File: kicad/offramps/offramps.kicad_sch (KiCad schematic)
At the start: 211 parts, among them J10 Conn_01x04_Socket, J11 Screw_Terminal_01x02, J12 Conn_01x04_Pin, J13 Micro_SD_Card, J14 Conn_01x03_Male, J15 Screw_Terminal_01x02, J16 Conn_01x02_Pin, J17 Conn_01x02_Pin, J3 VITA_57.1_FMC_HPC_Carrier, J4 Conn_01x02_Pin, J5 Conn_Coaxial, J6 Conn_01x03_Male, J7 Conn_Coaxial, J8 Conn_Coaxial, J9 Conn_01x06_Male, Q1 BSS138, Q10 BSS138, Q11 BSS138, Q12 BSS138, Q13 NPN, Q14 NPN, Q15 NPN, Q16 NPN, Q17 BSS138, Q2 BSS138, Q25 BSS138, Q26 BSS138, Q27 BSS138, Q28 BSS138, Q29 BSS138, Q3 BSS138, Q30 BSS138, Q4 BSS138, Q5 BSS138, Q6 BSS138, Q7 BSS138, Q8 BSS138, Q9 BSS138, SW1 219-8MST, U1 TXB0108PWR, U10 MCP4725xxx-xCH, U11 LMH6611MK/NOPB, U12 ADC1173CIMTC/NOPB, U13 MCP4725xxx-xCH, U14 POPA2994IDGKR, U15 ADS1114IDGS, U16 LIS2MDLTR, U17 LSM6DSRTR, U18 LTC-4627JR, U19 AMS1117-3.3, U2 TXB0108PWR, U20 LM358DR2G, U3 TXB0108PWR, U4 TXB0108PWR, U5 TXB0108PWR, U6 LMH6611MK/NOPB, U7 ADC1175CIMTC/NOPB, U8 TXB0108PWR, U9 PTMUX4053PWR

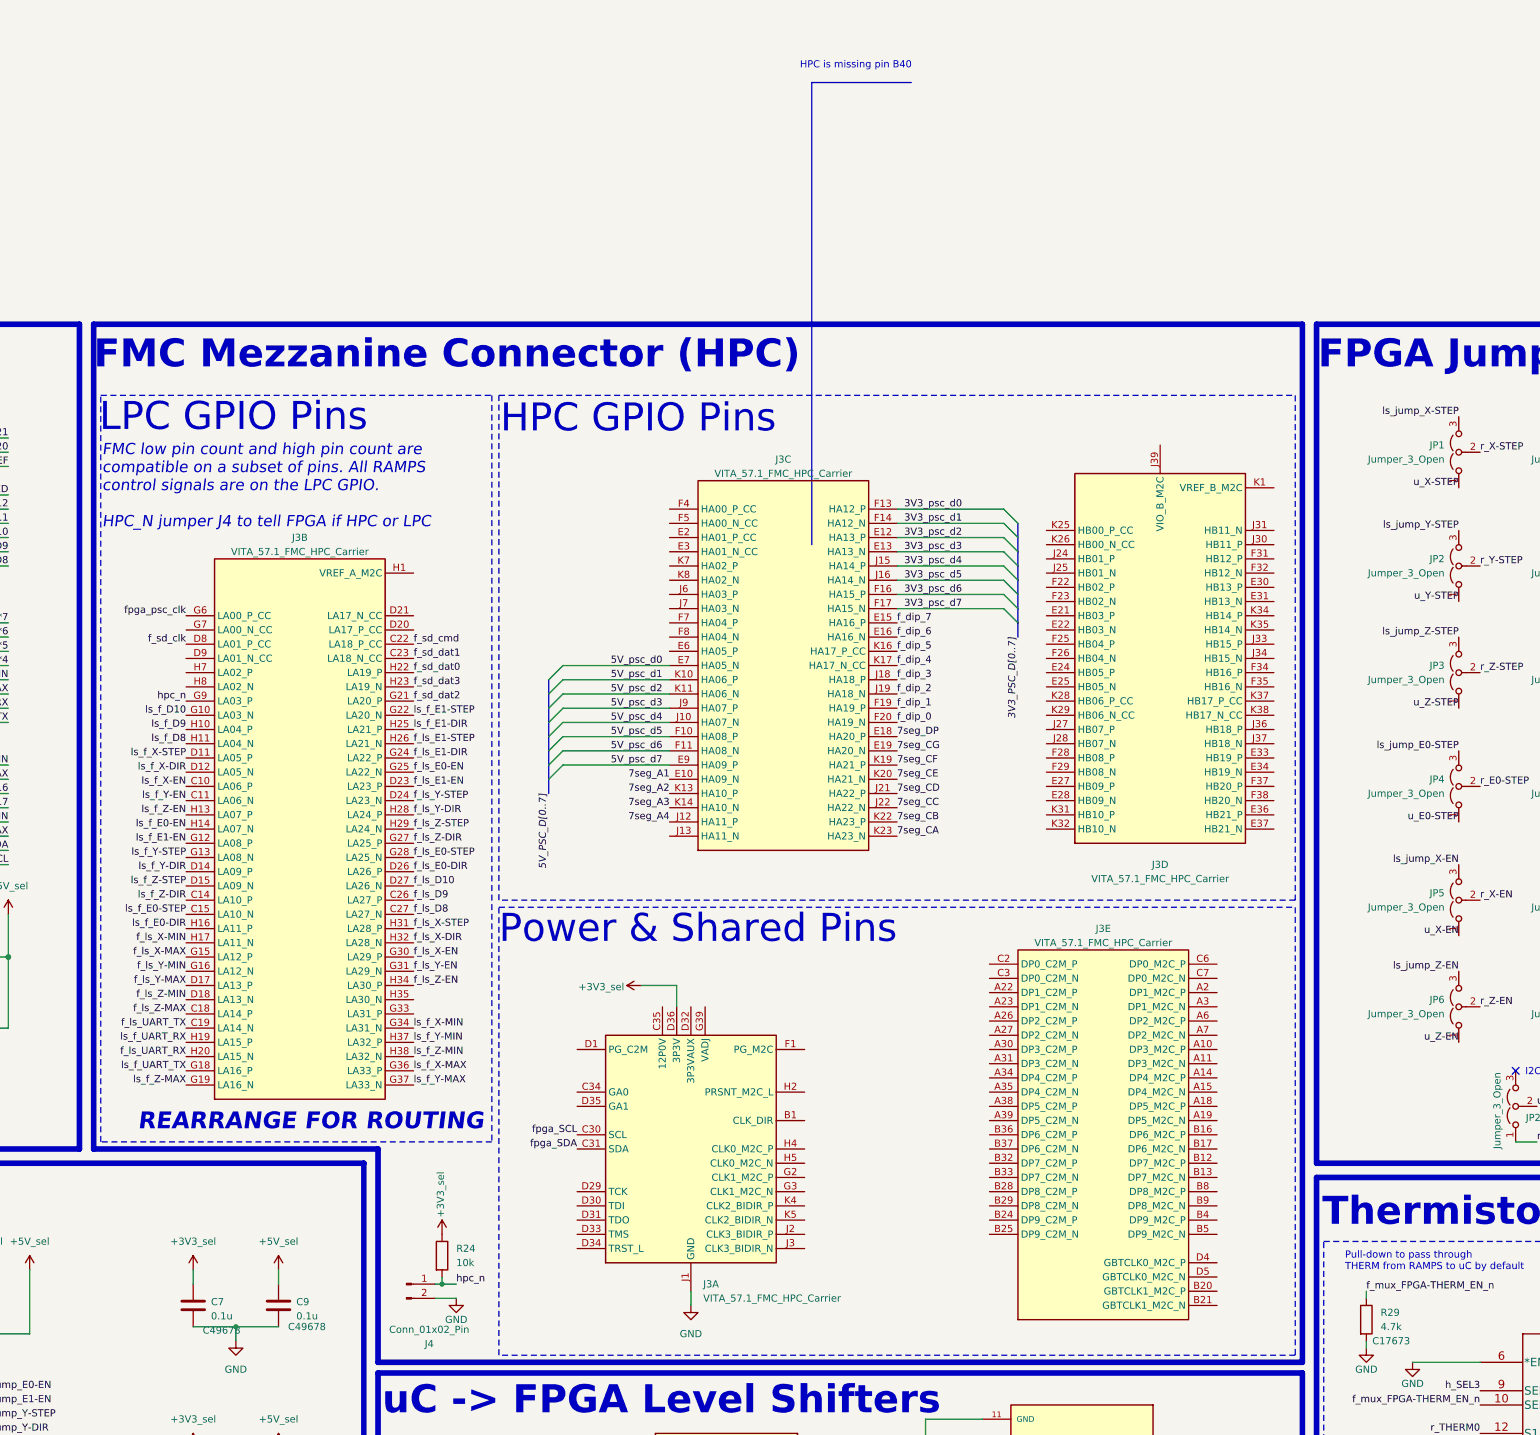
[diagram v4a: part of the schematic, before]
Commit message: Updates: FMC routing more or less complete
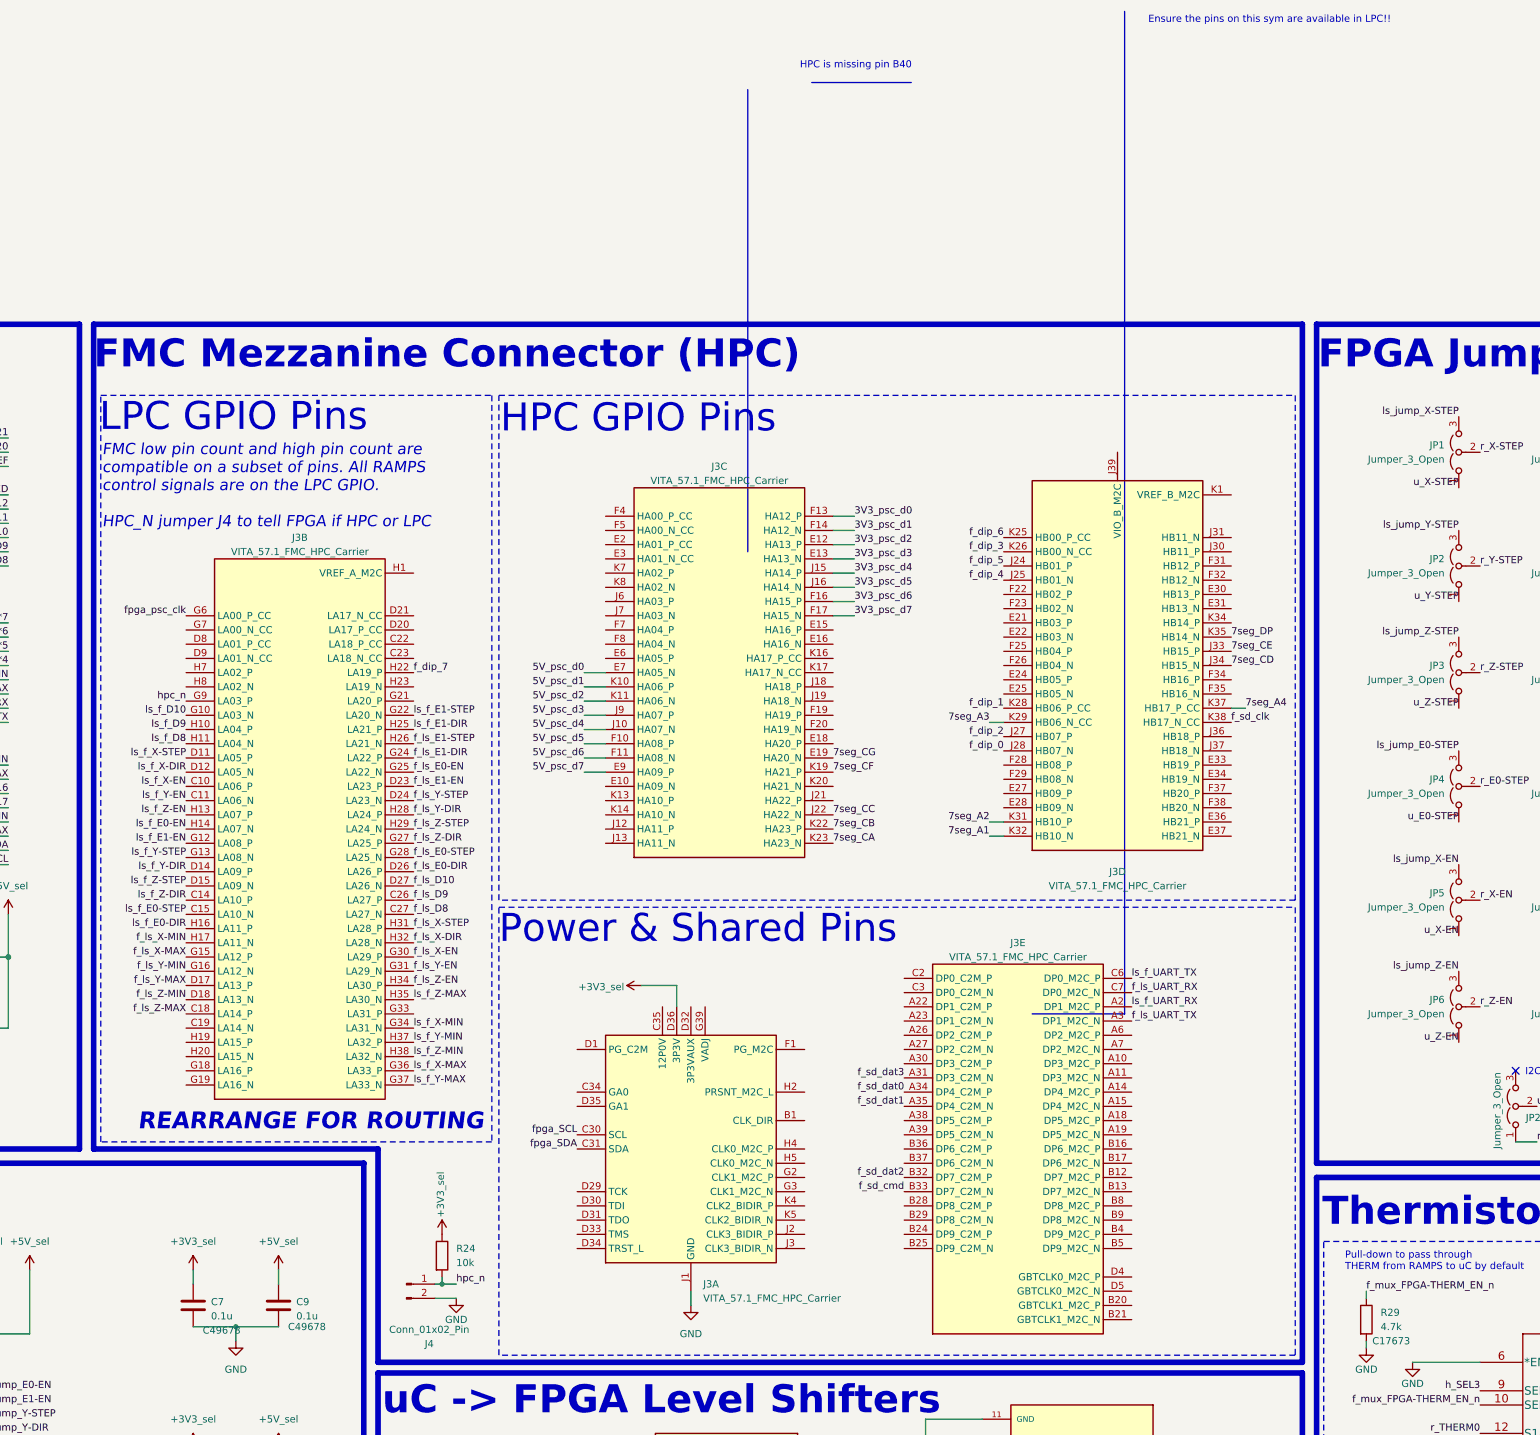
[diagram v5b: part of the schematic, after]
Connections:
- net 7seg_A1: now also J3.K32 (HB10_N); no longer J3.E10 (HA09_N)
- net 7seg_A2: now also J3.K31 (HB10_P); no longer J3.K13 (HA10_P)
- net 7seg_A3: now also J3.K29 (HB06_N_CC); no longer J3.K14 (HA10_N)
- net 7seg_A4: now also J3.K37 (HB17_P_CC); no longer J3.J12 (HA11_P)
- net 7seg_CD: now also J3.J34 (HB15_N); no longer J3.J21 (HA22_P)
- net 7seg_CE: now also J3.J33 (HB15_P); no longer J3.K20 (HA21_N)
- net 7seg_DP: now also J3.K35 (HB14_N); no longer J3.E18 (HA20_P)
- net f_dip_0: now also J3.J28 (HB07_N); no longer J3.F20 (HA19_N)
- net f_dip_1: now also J3.K28 (HB06_P_CC); no longer J3.F19 (HA19_P)
- net f_dip_2: now also J3.J27 (HB07_P); no longer J3.J19 (HA18_N)
- net f_dip_3: now also J3.K26 (HB00_N_CC); no longer J3.J18 (HA18_P)
- net f_dip_4: now also J3.J25 (HB01_N); no longer J3.K17 (HA17_N_CC)
- net f_dip_5: now also J3.J24 (HB01_P); no longer J3.K16 (HA17_P_CC)
- net f_dip_6: now also J3.K25 (HB00_P_CC); no longer J3.E16 (HA16_N)
- net f_dip_7: now also J3.H22 (LA19_P); no longer J3.E15 (HA16_P)
- net f_ls_UART_RX: now also J3.C7 (DP0_M2C_N); no longer J3.H20 (LA15_N)
- net f_ls_UART_TX: now also J3.A3 (DP1_M2C_N); no longer J3.C19 (LA14_N)
- net f_sd_clk: now also J3.K38 (HB17_N_CC); no longer J3.D8 (LA01_P_CC)
- net f_sd_cmd: now also J3.B33 (DP7_C2M_N); no longer J3.C22 (LA18_P_CC)
- net f_sd_dat0: now also J3.A34 (DP4_C2M_P); no longer J3.H22 (LA19_P)
- net f_sd_dat1: now also J3.A35 (DP4_C2M_N); no longer J3.C23 (LA18_N_CC)
- net f_sd_dat2: now also J3.B32 (DP7_C2M_P); no longer J3.G21 (LA20_P)
- net f_sd_dat3: now also J3.A31 (DP3_C2M_N); no longer J3.H23 (LA19_N)
- net ls_f_UART_RX: now also J3.A2 (DP1_M2C_P); no longer J3.H19 (LA15_P)
- net ls_f_UART_TX: now also J3.C6 (DP0_M2C_P); no longer J3.G18 (LA16_P)
- net ls_f_Z-MAX: now also J3.H35 (LA30_N); no longer J3.G19 (LA16_N)
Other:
- note added: "Ensure the pins on this sym are available in LPC!!"
- moved on the sheet: J3C, J3D, J3E

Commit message: Finished schematic for pcb layout (I hope...)
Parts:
- added C43, C44, C45, C46: 10u, symbol Device:C
- added Q18: BSS138, Package_TO_SOT_SMD:SOT-23, symbol Transistor_FET:BSS138
- added Q19: NPN, Package_TO_SOT_SMD:SOT-23, symbol Simulation_SPICE:NPN
- added R56, R66, R68, R71: 1k, symbol Device:R
- added R67, R69, R70, R78: 0, symbol Device:R
- added R79: 10k, Resistor_SMD:R_0805_2012Metric, symbol Device:R
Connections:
- net 5v_psc_ain is gone; now on net 5V_psc_ain: C15.1, R27.2, U6.1 (OUT)
- net +3V3_filt: now also C27.1, C28.1, C29.1, C30.1, C31.1, U12.11 (DVDD), U12.13 (DVDD), U12.14 (AVDD), U12.15 (AVDD), U12.18 (AVDD), C43.2, C46.2, R68.1, R71.1
- net +3V3_sel: now also Q19.3 (E)
- net +5V_filt: no longer C27.1, C28.1, C29.1, C30.1, C31.1, U12.11 (DVDD), U12.13 (DVDD), U12.14 (AVDD), U12.15 (AVDD), U12.18 (AVDD)
- net +5V_sel: now also Q18.3 (D)
- net 3V3_psc_oe_n: now also J3.E15 (HA16_P)
- net 5V_psc_oe_n: now also Q18.2 (S), R79.1
- net GND: now also C44.1, C45.1, R56.1, R66.1, R79.2
- net 7seg_L: now reaches J3.E28 (HB09_N)
- net 7seg_L: now also Q19.2 (B)
- net at U18.4 (CAL): now also Q19.1 (C)
- net at U12.16 (VRTS): now also R70.2
- net at U12.17 (VRT): now also C43.1, R70.1, R71.2
- net at U12.22 (VRBS): now also R67.2
- net at U12.23 (VRB): now also C44.2, R56.2, R67.1
- net at U7.16 (VRTS): now also R78.2
- net at U7.17 (VRT): now also C46.1, R68.2, R78.1
- net at U7.22 (VRBS): now also R69.2
- net at U7.23 (VRB): now also C45.2, R66.2, R69.1
- net fpga_5V_psc_oe_n: now reaches J3.E16 (HA16_N)
- net fpga_5V_psc_oe_n: now also Q18.1 (G)
- no-connect marks 9 -> 139
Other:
- note added: "5V output enable"
- note added: "fpga_control_pin"
- moved on the sheet: R28, U12A, U7A, U8

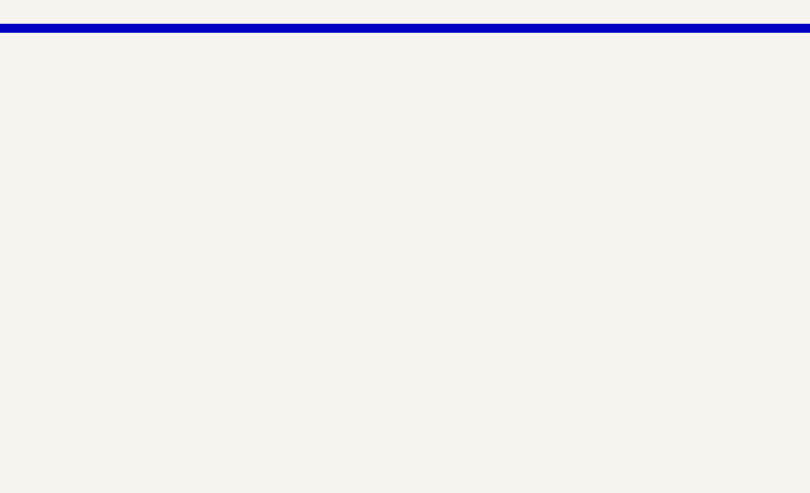
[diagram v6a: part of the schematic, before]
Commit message: Updates: Resize, Mounting Hole, E1 jumper, re-routing, moved screw terminal
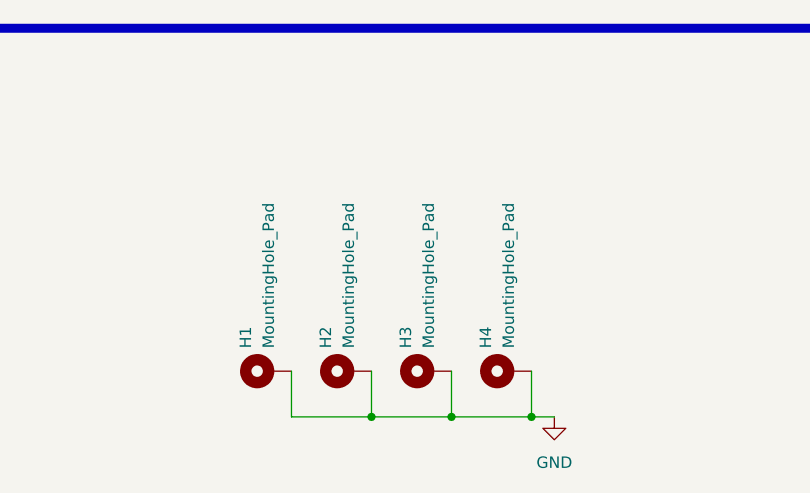
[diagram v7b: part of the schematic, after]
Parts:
- added H1, H2, H3, H4: MountingHole_Pad, MountingHole:MountingHole_3.2mm_M3_Pad, symbol Mechanical:MountingHole_Pad
- C43, C44, C45, C46: footprint (none) -> Capacitor_SMD:C_0805_2012Metric
- R56, R66, R67, R68, R69, R70, R71, R78: footprint (none) -> Resistor_SMD:R_0805_2012Metric
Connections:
- net GND: now also H1.1, H2.1, H3.1, H4.1

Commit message: Routing Complete. TODO: Listed in layout
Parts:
- removed TP1, TP2, TP3, TP4, TP5, TP6: TestPoint_Probe, TestPoint:TestPoint_Loop_D2.50mm_Drill1.0mm, symbol Connector:TestPoint_Probe
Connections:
- net 7seg_L: now also J3.J31 (HB11_N); no longer J3.E28 (HB09_N)
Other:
- note added: "to be added as needed"
- note removed: "To be added where needed during routing"
